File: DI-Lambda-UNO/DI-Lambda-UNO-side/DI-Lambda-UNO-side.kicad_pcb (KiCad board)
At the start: 2 copper layers, 125 x 28.2 mm, 0 parts

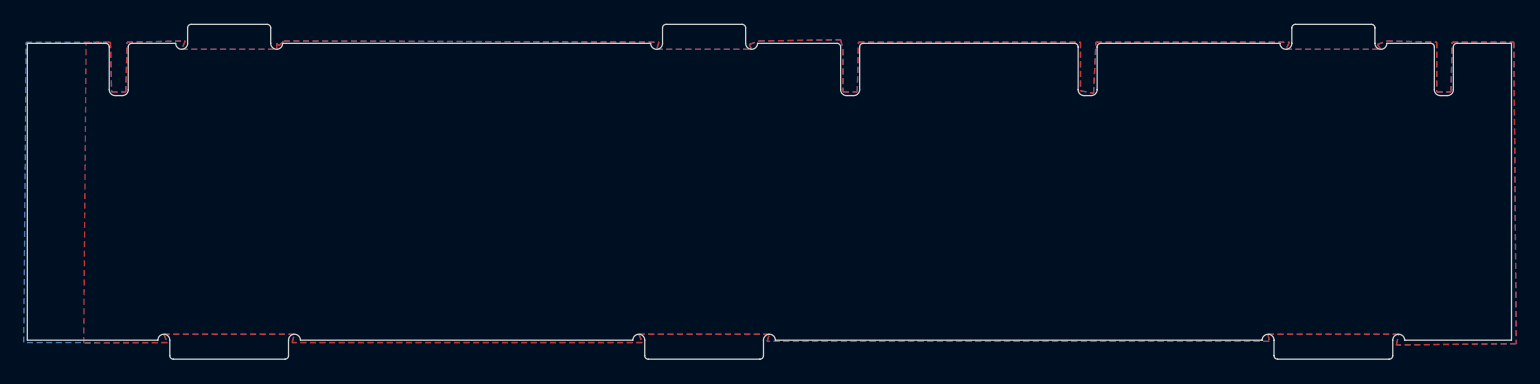
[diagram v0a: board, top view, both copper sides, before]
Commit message: Side board: Convert to 18mm height
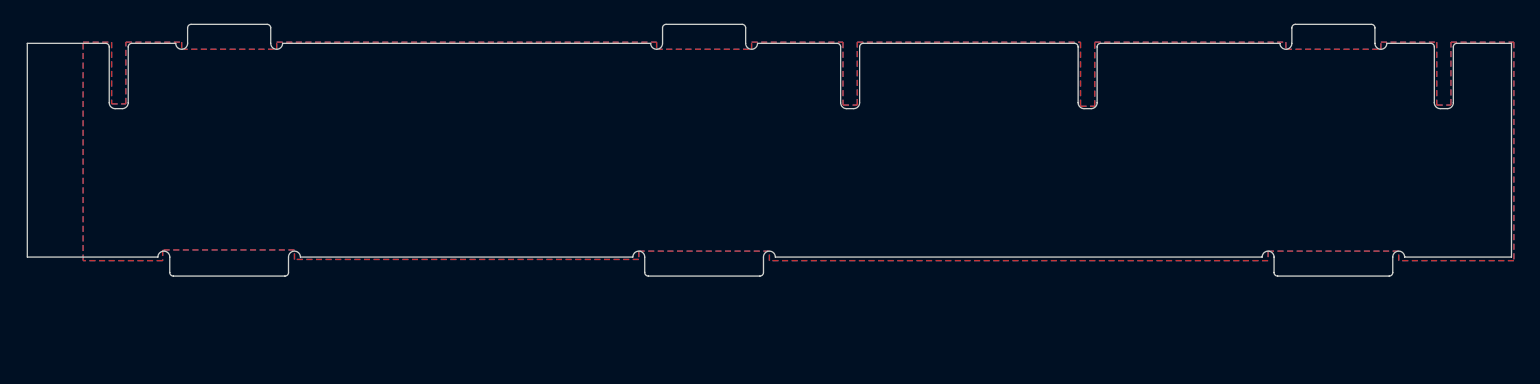
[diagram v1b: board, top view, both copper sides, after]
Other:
- board size 125 x 28.2 mm -> 125 x 21.2 mm
- board text added: "DI-Lambda UNO v1.3"
- board text removed: "DI-Lambda UNO v1.1"

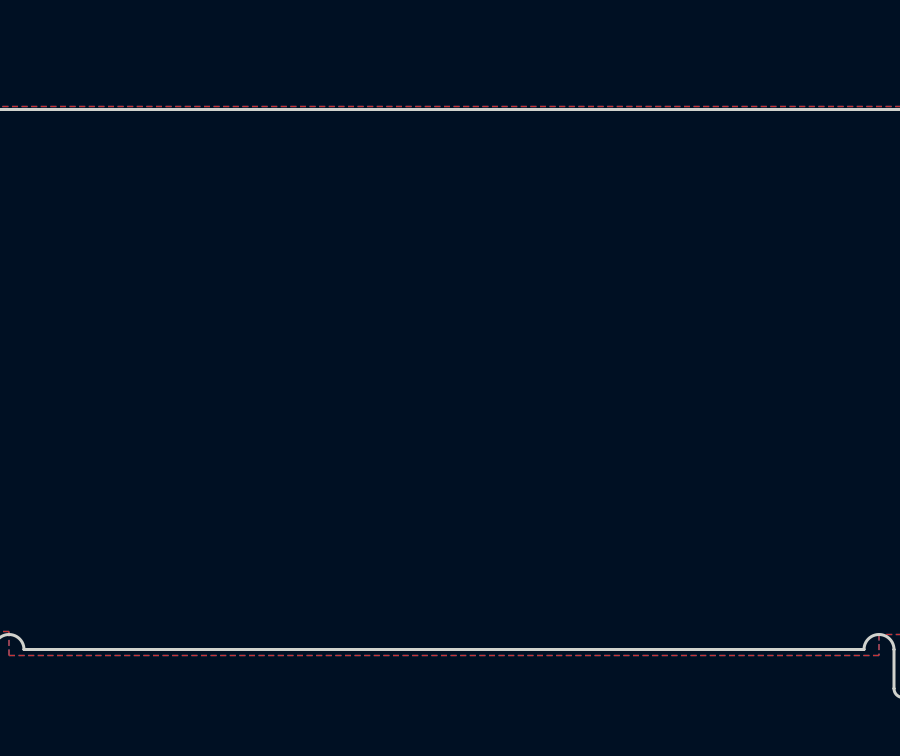
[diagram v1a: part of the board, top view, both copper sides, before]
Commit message: Update schematics to version 1.3
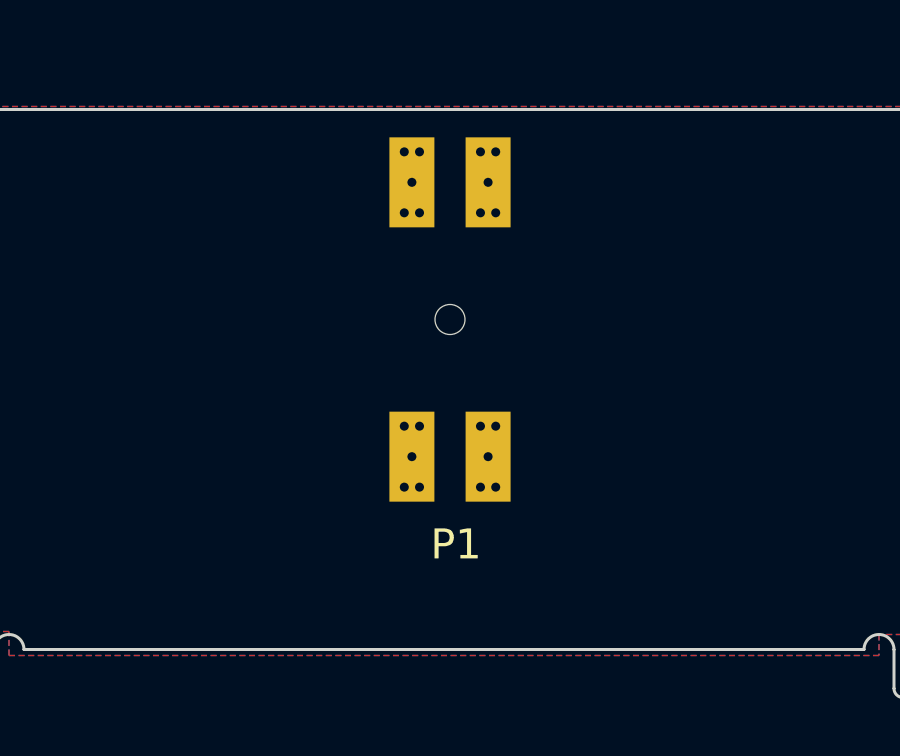
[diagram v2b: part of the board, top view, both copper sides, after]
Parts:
- added P1: CONN_02X02, Female_socket_pitch254_smt_through-board:Female_socket_2.54_2x4p_horizontal_smt, F.Cu at (132.3, 58.5)
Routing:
- added copper zone on B.Cu, net GND
- added copper zone on F.Cu, net GND
- removed copper zone on B.Cu, net (none)
- removed copper zone on F.Cu, net (none)
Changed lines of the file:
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@@
   (general
     (thickness 1.6)
-    (drawings 111)
+    (drawings 112)
     (tracks 0)
     (zones 0)
-    (modules 0)
-    (nets 1)
+    (modules 1)
+    (nets 2)
   )
   (page A4)
@@
     (40 Dwgs.User user)
     (41 Cmts.User user)
-    (42 Eco1.User user hide)
+    (42 Eco1.User user)
     (43 Eco2.User user)
     (44 Edge.Cuts user)
@@
     (visible_elements FFFDEF7F)
     (pcbplotparams
-      (layerselection 0x010c0_ffffffff)
+      (layerselection 0x010f0_ffffffff)
       (usegerberextensions true)
       (usegerberattributes true)
       (usegerberadvancedattributes true)
       (creategerberjobfile true)
-      (excludeedgelayer false)
+      (excludeedgelayer true)
       (linewidth 0.100000)
       (plotframeref false)
@@
       (drillshape 0)
       (scaleselection 1)
-      (outputdirectory DI-Lambda-UNO-side-v1.0-gerbers-2017oct25/))
+      (outputdirectory DI-Lambda-UNO-side-v1.3-gerbers-2017dec10/../))
   )
   (net 0 "")
+  (net 1 GND)
   (net_class Default "This is the default net class."
     (clearance 0.2)
@@
     (uvia_dia 0.3)
     (uvia_drill 0.1)
+    (add_net GND)
+  )
+  (module Female_socket_pitch254_smt_through-board:Female_socket_2.54_2x4p_horizontal_smt (layer F.Cu)
+    (at 132.28 58.51)
+    (fp_text reference P1 (at 0.2 7.5) (layer F.SilkS)
+      (effects (font (size 1 1) (thickness 0.15)))
+    )
+    (fp_text value CONN_02X02 (at -1 11.5) (layer F.Fab)
+      (effects (font (size 1 1) (thickness 0.15)))
+    )
+    (pad 3 thru_hole rect (at -1.27 -4.572) (size 1.5 3) (drill 0.3) (layers *.Cu *.Mask)
+      (net 1 GND))
+    (pad 1 thru_hole rect (at 1.27 -4.572) (size 1.5 3) (drill 0.3) (layers *.Cu *.Mask)
+      (net 1 GND))
+    (pad 4 thru_hole rect (at -1.27 4.572) (size 1.5 3) (drill 0.3) (layers *.Cu *.Mask)
+      (net 1 GND))
+    (pad 2 thru_hole rect (at 1.27 4.572) (size 1.5 3) (drill 0.3) (layers *.Cu *.Mask)
+      (net 1 GND))
+    (pad "" np_thru_hole circle (at 0 0) (size 1 1) (drill 1) (layers *.Cu *.Mask))
+    (pad 3 thru_hole circle (at -1.524 -3.556) (size 0.3 0.3) (drill 0.3) (layers *.Cu *.Mask)
+      (net 1 GND))
+    (pad 3 thru_hole circle (at -1.016 -3.556) (size 0.3 0.3) (drill 0.3) (layers *.Cu *.Mask)
+      (net 1 GND))
+    (pad 3 thru_hole circle (at -1.524 -5.588) (size 0.3 0.3) (drill 0.3) (layers *.Cu *.Mask)
+      (net 1 GND))
+    (pad 3 thru_hole circle (at -1.016 -5.588) (size 0.3 0.3) (drill 0.3) (layers *.Cu *.Mask)
+      (net 1 GND))
+    (pad 1 thru_hole circle (at 1.016 -3.556) (size 0.3 0.3) (drill 0.3) (layers *.Cu *.Mask)
+      (net 1 GND))
+    (pad 1 thru_hole circle (at 1.524 -3.556) (size 0.3 0.3) (drill 0.3) (layers *.Cu *.Mask)
+      (net 1 GND))
+    (pad 1 thru_hole circle (at 1.016 -5.588) (size 0.3 0.3) (drill 0.3) (layers *.Cu *.Mask)
+      (net 1 GND))
+    (pad 1 thru_hole circle (at 1.524 -5.588) (size 0.3 0.3) (drill 0.3) (layers *.Cu *.Mask)
+      (net 1 GND))
+    (pad 4 thru_hole circle (at -1.524 3.556) (size 0.3 0.3) (drill 0.3) (layers *.Cu *.Mask)
+      (net 1 GND))
+    (pad 4 thru_hole circle (at -1.016 3.556) (size 0.3 0.3) (drill 0.3) (layers *.Cu *.Mask)
+      (net 1 GND))
+    (pad 4 thru_hole circle (at -1.016 5.588) (size 0.3 0.3) (drill 0.3) (layers *.Cu *.Mask)
+      (net 1 GND))
+    (pad 4 thru_hole circle (at -1.524 5.588) (size 0.3 0.3) (drill 0.3) (layers *.Cu *.Mask)
+      (net 1 GND))
+    (pad 2 thru_hole circle (at 1.016 5.588) (size 0.3 0.3) (drill 0.3) (layers *.Cu *.Mask)
+      (net 1 GND))
+    (pad 2 thru_hole circle (at 1.524 5.588) (size 0.3 0.3) (drill 0.3) (layers *.Cu *.Mask)
+      (net 1 GND))
+    (pad 2 thru_hole circle (at 1.524 3.556) (size 0.3 0.3) (drill 0.3) (layers *.Cu *.Mask)
+      (net 1 GND))
+    (pad 2 thru_hole circle (at 1.016 3.556) (size 0.3 0.3) (drill 0.3) (layers *.Cu *.Mask)
+      (net 1 GND))
+  )
+  (dimension 28.7 (width 0.3) (layer Eco1.User)
+    (gr_text "28.700 mm" (at 117.93 45.46) (layer Eco1.User)
+      (effects (font (size 1.5 1.5) (thickness 0.3)))
+    )
+    (feature1 (pts (xy 132.28 52.41) (xy 132.28 44.11)))
+    (feature2 (pts (xy 103.58 52.41) (xy 103.58 44.11)))
+    (crossbar (pts (xy 103.58 46.81) (xy 132.28 46.81)))
+    (arrow1a (pts (xy 132.28 46.81) (xy 131.153496 47.396421)))
+    (arrow1b (pts (xy 132.28 46.81) (xy 131.153496 46.223579)))
+    (arrow2a (pts (xy 103.58 46.81) (xy 104.706504 47.396421)))
+    (arrow2b (pts (xy 103.58 46.81) (xy 104.706504 46.223579)))
   )
   (dimension 5.5 (width 0.3) (layer Eco1.User)
@@
   (gr_line (start 103.08 57.01) (end 102.48 57.01) (layer Edge.Cuts) (width 0.1))
   (gr_line (start 103.58 51.81) (end 103.58 56.51) (layer Edge.Cuts) (width 0.1))
-  (zone (net 0) (net_name "") (layer F.Cu) (hatch edge 0.508)
+  (zone (net 1) (net_name GND) (layer F.Cu) (hatch edge 0.508)
     (connect_pads (clearance 0.508))
     (min_thickness 0.254)
@@
     )
   )
-  (zone (net 0) (net_name "") (layer B.Cu) (hatch edge 0.508)
+  (zone (net 1) (net_name GND) (layer B.Cu) (hatch edge 0.508)
     (connect_pads (clearance 0.508))
     (min_thickness 0.254)

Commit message: Version 1.5 redesign WIP
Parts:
- added P2: CONN_01X04, Board_grooves:Tab_10mm_4pads_vias_3mm, F.Cu at (152.1, 76.5)
- added P3: CONN_01X04, Board_grooves:Tab_10mm_4pads_vias_3mm, F.Cu at (112.1, 76.5)
- added P4: CONN_01X04, Board_grooves:Tab_10mm_4pads_vias_3mm, F.Cu at (205.1, 76.5)
- moved P1 6.07 mm to (130.2, 64.2)
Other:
- board size 125 x 21.2 mm -> 125 x 30.2 mm
- board text added: "DI-Lambda UNO v1.5"
- board text removed: "DI-Lambda UNO v1.3"

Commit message: Version 1.5
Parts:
- added MK1: Mounting_Hole, Board_grooves:Tab_7mm_1.5mm, F.Cu at (152.1, 51.5)
- added MK2: Mounting_Hole, Board_grooves:Tab_7mm_1.5mm, F.Cu at (112.1, 51.5)
- added MK3: Mounting_Hole, Board_grooves:Tab_7mm_1.5mm, F.Cu at (205.1, 51.5)
- added P5: CONN_02X02, Female_socket_pitch254_smt_through-board:Female_socket_2.54_2x2p_horizontal_smt, F.Cu at (122.1, 59.5)
- added P6: CONN_02X02, Female_socket_pitch254_smt_through-board:Female_socket_2.54_2x2p_horizontal_smt, F.Cu at (195.1, 59.5)
- P1: footprint Female_socket_pitch254_smt_through-board:Female_socket_2.54_2x4p_horizontal_smt -> Female_socket_pitch254_smt_through-board:Female_socket_2.54_2x2p_horizontal_smt
- P3: footprint Board_grooves:Tab_10mm_4pads_vias_3mm -> Board_grooves:Tab_10mm_3pads_vias_3mm
- moved P2 40.0 mm to (112.1, 76.5)
- moved P3 40.0 mm to (152.1, 76.5)
- moved P1 4.70 mm to (132.1, 68.5), turned to 180 degrees
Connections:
- P1 pad 1: GND -> /A-
- P1 pad 2: GND -> /B+
- P1 pad 3: GND -> /A+
- P1 pad 4: GND -> /B-
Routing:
- net /A-: track 0.00 -> 31.1 mm
- net /A+: track 0.00 -> 31.1 mm
- net /B-: track 0.00 -> 12.5 mm
- net /B+: track 0.00 -> 12.5 mm
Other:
- board size 125 x 30.2 mm -> 128 x 25 mm

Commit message: Version 1.6
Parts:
- added MK4: Mounting_Hole, Cuvette-holder:Cuvette_holder_side_hole, F.Cu at (174.4, 68.5)
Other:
- outline, holes or cut-outs redrawn
- board text added: "DI-Lambda UNO v1.6"
- board text removed: "DI-Lambda UNO v1.5"

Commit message: More missing fotprints
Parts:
- moved MK303 232.2 mm to (-25.0, 20.0), turned to 270 degrees
- moved P302 214.1 mm to (-17.0, 30.0), turned to 90 degrees
- moved P306 212.7 mm to (0.00, 20.0), turned to 90 degrees
- moved MK304 183.3 mm to (-8.05, 50.7), turned to 90 degrees
- moved MK301 178.4 mm to (-25.0, 73.0), turned to 270 degrees
- moved P305 152.1 mm to (0.00, 73.0), turned to 90 degrees
- moved MK302 150.2 mm to (-25.0, 113.0), turned to 270 degrees
- moved P301 145.7 mm to (-17.0, 103.0), turned to 90 degrees
- moved P303 142.2 mm to (-8.00, 93.0), turned to 270 degrees
- moved P304 117.9 mm to (0.00, 113.0), turned to 90 degrees
- renumbered MK1 to MK301, MK2 to MK302, MK3 to MK303, MK4 to MK304, P5 to P301, P6 to P302, P1 to P303, P2 to P304, P3 to P305, P4 to P306
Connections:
- P304 pad 1: GND -> Net-(P304-Pad1)
- P304 pad 2: GND -> Net-(P304-Pad2)
- P304 pad 3: GND -> Net-(P304-Pad3)
- P304 pad 4: GND -> Net-(P304-Pad4)
- P305 pad 1: GND -> Net-(P305-Pad1)
- P305 pad 2: GND -> Net-(P305-Pad2)
- P305 pad 3: GND -> Net-(P305-Pad3)
- P306 pad 1: GND -> Net-(P306-Pad1)
- P306 pad 2: GND -> Net-(P306-Pad2)
- P306 pad 3: GND -> Net-(P306-Pad3)
- P306 pad 4: GND -> Net-(P306-Pad4)
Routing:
- net GND: track 0.00 -> 1.76 mm
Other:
- board size 128 x 25 mm -> 25 x 128 mm
- board text added: "DI-Lambda UNO v1.7"
- board text removed: "DI-Lambda UNO v1.6"
